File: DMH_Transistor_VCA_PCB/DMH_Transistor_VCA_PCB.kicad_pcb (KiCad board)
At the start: 2 copper layers, 48 x 175 mm, 0 parts

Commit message: Finished main PCB
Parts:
- added C1: 47uF, Capacitor_THT:CP_Radial_D5.0mm_P2.00mm, B.Cu at (73.3, 57.5)
- added C2: 47uF, Capacitor_THT:CP_Radial_D5.0mm_P2.00mm, B.Cu at (90.8, 57.5)
- added C3: 100nF, Capacitor_THT:C_Disc_D4.3mm_W1.9mm_P5.00mm, B.Cu at (69.2, 56.8)
- added C4: 100nF, Capacitor_THT:C_Disc_D4.3mm_W1.9mm_P5.00mm, B.Cu at (97.0, 61.8)
- added C5: 100nF, Capacitor_THT:C_Disc_D4.3mm_W1.9mm_P5.00mm, B.Cu at (89.8, 79.2)
- added C6: 100nF, Capacitor_THT:C_Disc_D4.3mm_W1.9mm_P5.00mm, B.Cu at (76.2, 84.2)
- added C7: 100nF, Capacitor_THT:C_Disc_D4.3mm_W1.9mm_P5.00mm, B.Cu at (89.8, 170.0)
- added C8: 100nF, Capacitor_THT:C_Disc_D4.3mm_W1.9mm_P5.00mm, B.Cu at (76.2, 175.0)
- added D1: SB140+, Diode_THT:D_DO-41_SOD81_P10.16mm_Horizontal, B.Cu at (69.2, 54.3)
- added D2: SB140-, Diode_THT:D_DO-41_SOD81_P10.16mm_Horizontal, B.Cu at (97.0, 44.2)
- added J1: TS_Jack_6.35mm_Sw, SynthStuff:CUI_MJ-63052A, F.Cu at (58.5, 50.8)
- added J100: IDC_02x05, SynthStuff:IDC-Header_2x05_P2.54mm_Vertical_Eurorack, B.Cu at (88.1, 49.0)
- added J2: TS_Jack_6.35mm_Sw, SynthStuff:CUI_MJ-63052A, F.Cu at (58.5, 69.2)
- added J200: IDC_02x05, SynthStuff:IDC-Header_2x05_P2.54mm_Vertical_BackBone, B.Cu at (77.9, 138.2)
- added J3: TS_Jack_6.35mm_Sw, SynthStuff:CUI_MJ-63052A, F.Cu at (63.0, 118.0)
- added J4: TS_Jack_6.35mm_Sw, SynthStuff:CUI_MJ-63052A, F.Cu at (87.0, 118.0)
- added J5: TS_Jack_6.35mm_Sw, SynthStuff:CUI_MJ-63052A, F.Cu at (58.5, 141.5)
- added J50: Conn_01x05, Connector_PinSocket_2.54mm:PinSocket_1x05_P2.54mm_Vertical, F.Cu at (97.0, 76.1)
- added J6: TS_Jack_6.35mm_Sw, SynthStuff:CUI_MJ-63052A, F.Cu at (58.5, 160.0)
- added J60: Conn_01x05, Connector_PinSocket_2.54mm:PinSocket_1x05_P2.54mm_Vertical, F.Cu at (53.0, 187.9)
- added J7: TS_Jack_6.35mm_Sw, SynthStuff:CUI_MJ-63052A, F.Cu at (63.0, 208.8)
- added J8: TS_Jack_6.35mm_Sw, SynthStuff:CUI_MJ-63052A, F.Cu at (87.0, 208.8)
- added Q1: BC548, Package_TO_SOT_THT:TO-92L_Inline_Wide, B.Cu at (81.0, 103.5)
- added Q2: BC548, Package_TO_SOT_THT:TO-92L_Inline_Wide, B.Cu at (85.0, 108.5)
- added Q3: BC548, Package_TO_SOT_THT:TO-92L_Inline_Wide, B.Cu at (85.0, 199.3)
- added Q4: BC548, Package_TO_SOT_THT:TO-92L_Inline_Wide, B.Cu at (81.0, 194.2)
- added R1: 100k, Resistor_THT:R_Axial_DIN0207_L6.3mm_D2.5mm_P7.62mm_Horizontal, B.Cu at (79.2, 63.0)
- added R10: 100R, Resistor_THT:R_Axial_DIN0207_L6.3mm_D2.5mm_P7.62mm_Horizontal, B.Cu at (79.2, 92.7)
- added R11: 100k, Resistor_THT:R_Axial_DIN0207_L6.3mm_D2.5mm_P7.62mm_Horizontal, B.Cu at (75.3, 100.2)
- added R12: 100k, Resistor_THT:R_Axial_DIN0207_L6.3mm_D2.5mm_P7.62mm_Horizontal, B.Cu at (86.8, 92.7)
- added R13: 100R, Resistor_THT:R_Axial_DIN0207_L6.3mm_D2.5mm_P7.62mm_Horizontal, B.Cu at (83.0, 92.7)
- added R14: 20k, Resistor_THT:R_Axial_DIN0207_L6.3mm_D2.5mm_P7.62mm_Horizontal, B.Cu at (94.2, 108.6)
- added R15: 20k, Resistor_THT:R_Axial_DIN0207_L6.3mm_D2.5mm_P7.62mm_Horizontal, B.Cu at (90.8, 108.6)
- added R16: 10k, Resistor_THT:R_Axial_DIN0207_L6.3mm_D2.5mm_P7.62mm_Horizontal, B.Cu at (72.8, 76.7)
- added R17: 10k, Resistor_THT:R_Axial_DIN0207_L6.3mm_D2.5mm_P7.62mm_Horizontal, B.Cu at (69.5, 76.7)
- added R18: 100k, Resistor_THT:R_Axial_DIN0207_L6.3mm_D2.5mm_P7.62mm_Horizontal, B.Cu at (76.0, 65.2)
- added R19: 100k, Resistor_THT:R_Axial_DIN0207_L6.3mm_D2.5mm_P7.62mm_Horizontal, B.Cu at (69.5, 72.8)
- added R2: 100k, Resistor_THT:R_Axial_DIN0207_L6.3mm_D2.5mm_P7.62mm_Horizontal, B.Cu at (86.8, 69.5)
- added R20: 1k, Resistor_THT:R_Axial_DIN0207_L6.3mm_D2.5mm_P7.62mm_Horizontal, B.Cu at (72.8, 72.8)
- added R22: 20k, Resistor_THT:R_Axial_DIN0207_L6.3mm_D2.5mm_P7.62mm_Horizontal, B.Cu at (91.5, 155.7)
- added R23: 20k, Resistor_THT:R_Axial_DIN0207_L6.3mm_D2.5mm_P7.62mm_Horizontal, B.Cu at (94.8, 155.7)
- added R24: 100k, Resistor_THT:R_Axial_DIN0207_L6.3mm_D2.5mm_P7.62mm_Horizontal, B.Cu at (79.2, 160.2)
- added R25: 100k, Resistor_THT:R_Axial_DIN0207_L6.3mm_D2.5mm_P7.62mm_Horizontal, B.Cu at (69.0, 155.9)
- added R26: 10k, Resistor_THT:R_Axial_DIN0207_L6.3mm_D2.5mm_P7.62mm_Horizontal, B.Cu at (69.0, 167.4)
- added R27: 100k, Resistor_THT:R_Axial_DIN0207_L6.3mm_D2.5mm_P7.62mm_Horizontal, B.Cu at (86.8, 157.0)
- added R28: 100k, Resistor_THT:R_Axial_DIN0207_L6.3mm_D2.5mm_P7.62mm_Horizontal, B.Cu at (86.8, 153.8)
- added R29: 1k, Resistor_THT:R_Axial_DIN0207_L6.3mm_D2.5mm_P7.62mm_Horizontal, B.Cu at (75.5, 155.9)
- added R3: 100k, Resistor_THT:R_Axial_DIN0207_L6.3mm_D2.5mm_P7.62mm_Horizontal, B.Cu at (86.8, 66.2)
- added R30: 10k, Resistor_THT:R_Axial_DIN0207_L6.3mm_D2.5mm_P7.62mm_Horizontal, B.Cu at (72.2, 163.6)
- added R31: 100k, Resistor_THT:R_Axial_DIN0207_L6.3mm_D2.5mm_P7.62mm_Horizontal, B.Cu at (72.2, 167.4)
- added R32: 100k, Resistor_THT:R_Axial_DIN0207_L6.3mm_D2.5mm_P7.62mm_Horizontal, B.Cu at (90.0, 186.6)
- added R33: 100k, Resistor_THT:R_Axial_DIN0207_L6.3mm_D2.5mm_P7.62mm_Horizontal, B.Cu at (86.2, 190.8)
- added R34: 100k, Resistor_THT:R_Axial_DIN0207_L6.3mm_D2.5mm_P7.62mm_Horizontal, B.Cu at (83.0, 183.2)
- added R35: 100R, Resistor_THT:R_Axial_DIN0207_L6.3mm_D2.5mm_P7.62mm_Horizontal, B.Cu at (73.8, 190.9)
- added R36: 100R, Resistor_THT:R_Axial_DIN0207_L6.3mm_D2.5mm_P7.62mm_Horizontal, B.Cu at (79.8, 183.2)
- added R37: 100k, Resistor_THT:R_Axial_DIN0207_L6.3mm_D2.5mm_P7.62mm_Horizontal, B.Cu at (93.2, 186.6)
- added R38: 100k, Resistor_THT:R_Axial_DIN0207_L6.3mm_D2.5mm_P7.62mm_Horizontal, B.Cu at (96.5, 178.9)
- added R39: 10k, Resistor_THT:R_Axial_DIN0207_L6.3mm_D2.5mm_P7.62mm_Horizontal, B.Cu at (75.5, 178.9)
- added R4: 100k, Resistor_THT:R_Axial_DIN0207_L6.3mm_D2.5mm_P7.62mm_Horizontal, B.Cu at (90.0, 88.2)
- added R41: 82k, Resistor_THT:R_Axial_DIN0207_L6.3mm_D2.5mm_P7.62mm_Horizontal, B.Cu at (72.2, 186.6)
- added R42: 100k, Resistor_THT:R_Axial_DIN0207_L6.3mm_D2.5mm_P7.62mm_Horizontal, B.Cu at (69.0, 178.9)
- added R5: 100k, Resistor_THT:R_Axial_DIN0207_L6.3mm_D2.5mm_P7.62mm_Horizontal, B.Cu at (93.2, 95.8)
- added R6: 100k, Resistor_THT:R_Axial_DIN0207_L6.3mm_D2.5mm_P7.62mm_Horizontal, B.Cu at (96.5, 95.8)
- added R7: 100k, Resistor_THT:R_Axial_DIN0207_L6.3mm_D2.5mm_P7.62mm_Horizontal, B.Cu at (69.5, 95.8)
- added R8: 82k, Resistor_THT:R_Axial_DIN0207_L6.3mm_D2.5mm_P7.62mm_Horizontal, B.Cu at (76.0, 88.2)
- added R9: 10k, Resistor_THT:R_Axial_DIN0207_L6.3mm_D2.5mm_P7.62mm_Horizontal, B.Cu at (72.8, 88.2)
- added RV4: 100k, Potentiometer_THT:Potentiometer_Bourns_3296W_Vertical, B.Cu at (92.2, 64.5)
- added RV6: 100k, Potentiometer_THT:Potentiometer_Bourns_3296W_Vertical, B.Cu at (95.5, 168.5)
- added U1: TL074, Package_DIP:DIP-14_W7.62mm_Socket, B.Cu at (86.8, 72.9)
- added U2: TL074, Package_DIP:DIP-14_W7.62mm_Socket, B.Cu at (86.8, 163.6)
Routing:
- net -12V: track 0.00 -> 183.8 mm
- net +12V: track 0.00 -> 164.6 mm
- net Net-(J200-Pin_2): track 0.00 -> 126.8 mm
- net /Core Circuit B/CV 1 B Input: track 0.00 -> 101.6 mm
- net Net-(J200-Pin_1): track 0.00 -> 101.0 mm
- net Net-(J200-Pin_7): track 0.00 -> 88.2 mm
- net /Core Circuit B/CV 2 B Pot: track 0.00 -> 81.8 mm
- net Net-(Q4-C): track 0.00 -> 80.9 mm
- net Net-(Q1-C): track 0.00 -> 79.5 mm
- net Net-(J200-Pin_6): track 0.00 -> 78.1 mm
- net Net-(Q3-C): track 0.00 -> 76.3 mm
- net Net-(Q2-C): track 0.00 -> 65.3 mm
- net Net-(U2C--): track 0.00 -> 65.1 mm
- net Net-(U1C--): track 0.00 -> 62.6 mm
- net /Core Circuit B/Input B: track 0.00 -> 61.5 mm
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- added copper zone on B.Cu, net GND
- added copper zone on F.Cu, net GND

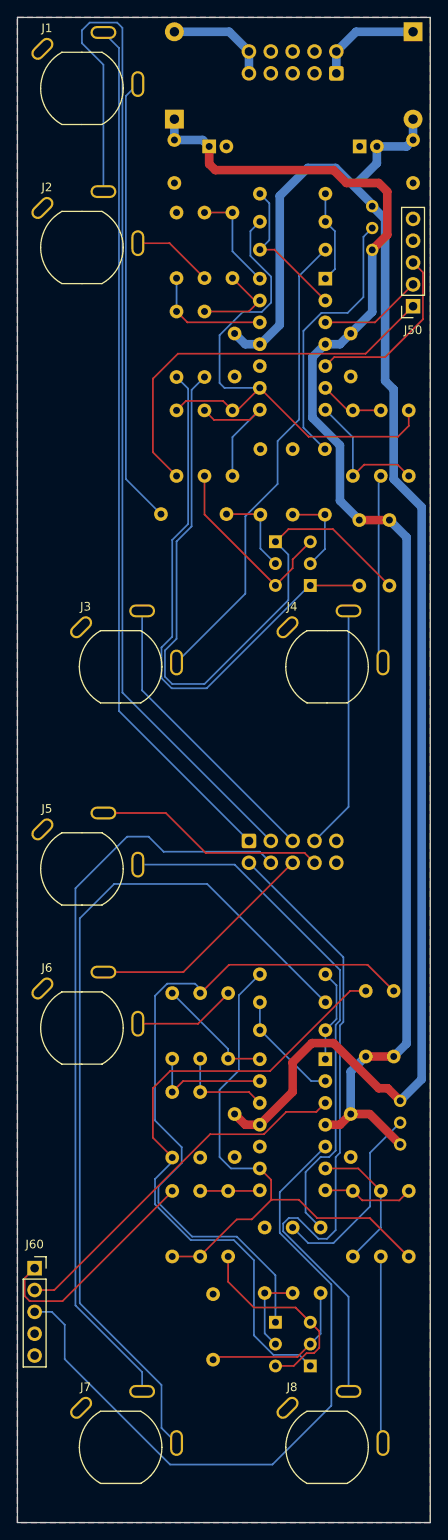
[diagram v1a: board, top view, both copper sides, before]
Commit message: Pots PCB in progress
Need to add CV input traces to the pin headers
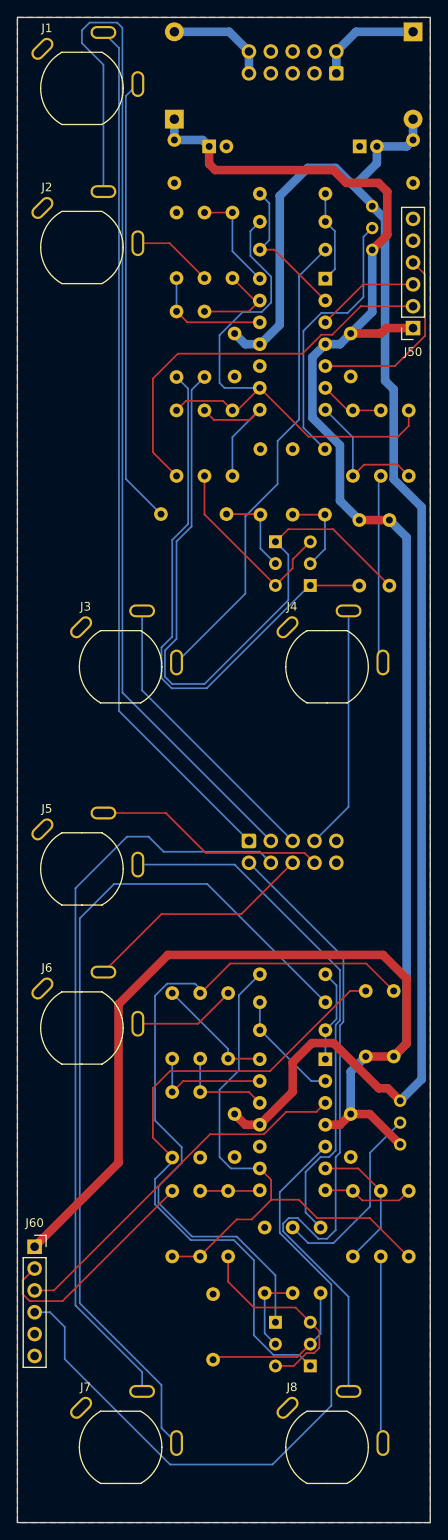
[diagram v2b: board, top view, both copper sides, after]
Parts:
- J50, J60: value Conn_01x05 -> Conn_01x06; footprint Connector_PinSocket_2.54mm:PinSocket_1x05_P2.54mm_Vertical -> Connector_PinSocket_2.54mm:PinSocket_1x06_P2.54mm_Vertical
- moved J50 2.54 mm to (97.0, 78.6)
- moved J60 2.49 mm to (53.0, 185.4)
- renumbered RV4 to RV7, RV6 to RV8
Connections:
- J50 pad 1: /Core Circuit A/Offset A Pot -> +12V
- J50 pad 2: /Core Circuit A/CV 1 A Pot -> /Core Circuit A/Offset A Pot
- J50 pad 3: /Core Circuit A/CV 2 A Pot -> /Core Circuit A/CV 1 A Pot
- J50 pad 4: GND -> /Core Circuit A/CV 2 A Pot
- J60 pad 1: /Core Circuit B/Offset B Pot -> +12V
- J60 pad 2: /Core Circuit B/CV 1 B Pot -> /Core Circuit B/Offset B Pot
- J60 pad 3: /Core Circuit B/CV 2 B Pot -> /Core Circuit B/CV 1 B Pot
- J60 pad 4: GND -> /Core Circuit B/CV 2 B Pot
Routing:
- net +12V: track 164.6 -> 251.0 mm
- net /Core Circuit A/CV 2 A Pot: track 20.7 -> 22.2 mm

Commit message: Finished Pots PCB
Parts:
- J50, J60: value Conn_01x06 -> Conn_01x08; footprint Connector_PinSocket_2.54mm:PinSocket_1x06_P2.54mm_Vertical -> Connector_PinSocket_2.54mm:PinSocket_1x08_P2.54mm_Vertical
- moved J60 5.05 mm to (53.0, 180.4)
- moved J50 5.00 mm to (97.0, 83.6)
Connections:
- J50 pad 1: +12V -> /Core Circuit A/CV 1 A Input
- J50 pad 2: /Core Circuit A/Offset A Pot -> /Core Circuit A/CV 2 A Input
- J50 pad 3: /Core Circuit A/CV 1 A Pot -> +12V
- J50 pad 4: /Core Circuit A/CV 2 A Pot -> /Core Circuit A/Offset A Pot
- J50 pad 5: GND -> /Core Circuit A/CV 1 A Pot
- J50 pad 6: GND -> /Core Circuit A/CV 2 A Pot
- J60 pad 1: +12V -> /Core Circuit B/CV 1 B Input
- J60 pad 2: /Core Circuit B/Offset B Pot -> /Core Circuit B/CV 2 B Input
- J60 pad 3: /Core Circuit B/CV 1 B Pot -> +12V
- J60 pad 4: /Core Circuit B/CV 2 B Pot -> /Core Circuit B/Offset B Pot
- J60 pad 5: GND -> /Core Circuit B/CV 1 B Pot
- J60 pad 6: GND -> /Core Circuit B/CV 2 B Pot
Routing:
- net /Core Circuit B/CV 2 B Input: track 21.8 -> 98.6 mm
- net /Core Circuit A/CV 1 A Input: track 55.2 -> 112.9 mm
- net /Core Circuit B/CV 1 B Input: track 101.6 -> 136.7 mm
- net /Core Circuit A/CV 2 A Input: track 22.0 -> 43.4 mm

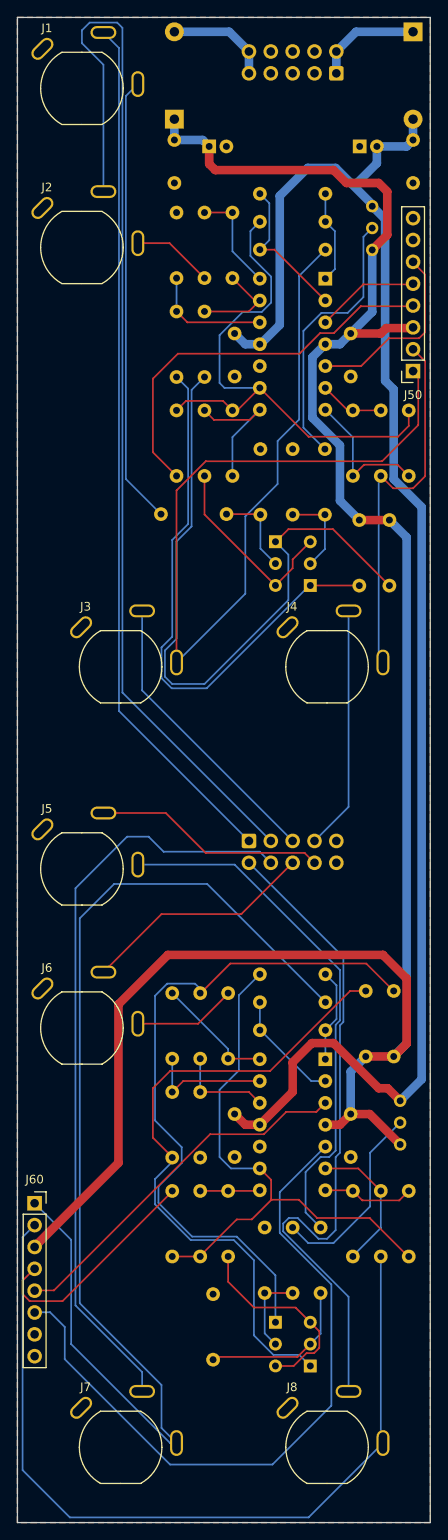
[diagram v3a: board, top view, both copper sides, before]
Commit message: Added CV input attenuverter adjustment trimpots
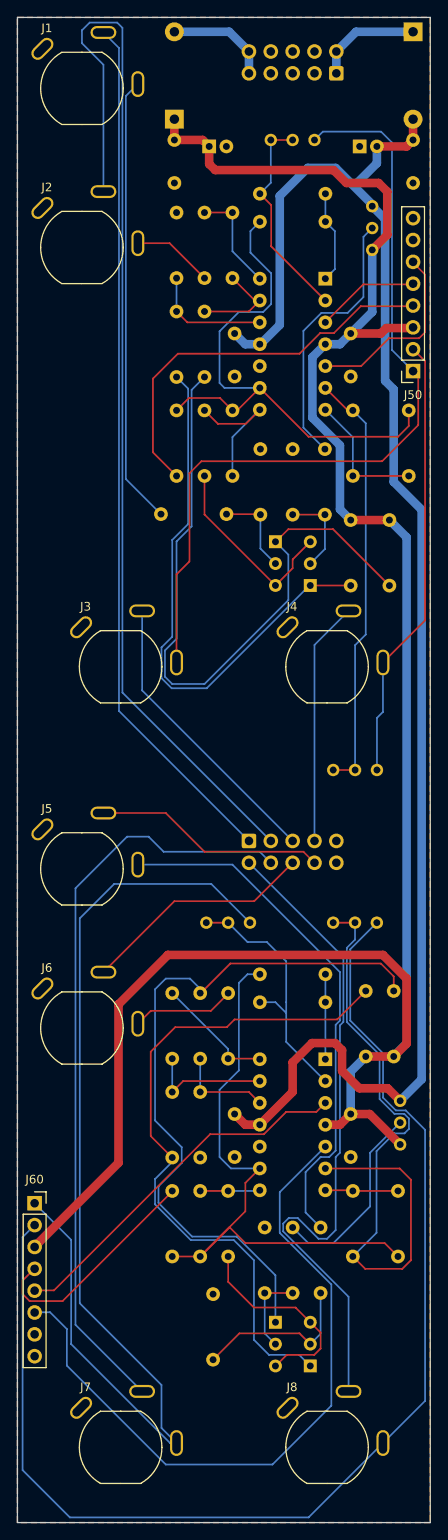
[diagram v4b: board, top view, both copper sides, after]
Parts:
- removed R2, R27, R37, R5: 100k, Resistor_THT:R_Axial_DIN0207_L6.3mm_D2.5mm_P7.62mm_Horizontal
- added RV10: 50k, Potentiometer_THT:Potentiometer_Bourns_3296W_Vertical, B.Cu at (92.8, 130.0)
- added RV11: 50k, Potentiometer_THT:Potentiometer_Bourns_3296W_Vertical, B.Cu at (78.0, 147.8)
- added RV12: 50k, Potentiometer_THT:Potentiometer_Bourns_3296W_Vertical, B.Cu at (92.8, 147.8)
- added RV9: 50k, Potentiometer_THT:Potentiometer_Bourns_3296W_Vertical, B.Cu at (85.5, 56.8)
- R1, R24, R32, R4: value 100k -> 33k
- moved R24 3.25 mm to (79.2, 157.0)
- moved R38 1.25 mm to (95.2, 178.9)
- moved R15 1.00 mm to (89.8, 108.6)
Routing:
- net Net-(U2B--): track 16.5 -> 76.4 mm
- net /Core Circuit B/CV 2 B Input: track 98.6 -> 144.9 mm
- net Net-(U1B--): track 7.53 -> 49.8 mm
- net Net-(U2A--): track 13.3 -> 30.5 mm
- net /Core Circuit A/CV 1 A Input: track 112.9 -> 95.8 mm
- net /Core Circuit B/CV 1 B Input: track 136.7 -> 124.1 mm
- net /Core Circuit A/CV 2 A Input: track 43.4 -> 51.5 mm
- net Net-(U1A--): track 17.5 -> 25.1 mm
- net Net-(U2C--): track 65.1 -> 71.4 mm
- net Net-(Q3-C): track 76.3 -> 79.0 mm
- net Net-(R32-Pad2): track 10.6 -> 8.48 mm
- net Net-(Q4-C): track 81.0 -> 82.9 mm
- net -12V: track 183.8 -> 185.2 mm
- net Net-(R4-Pad2): track 16.6 -> 15.5 mm
- net Net-(R24-Pad2): track 10.9 -> 9.88 mm
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
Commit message: Switched attenuverters trimpot and Rf positions
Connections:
- R1 pad 1: Net-(U1A--) -> /Core Circuit A/CV 1 A Input
- R1 pad 2: Net-(R1-Pad2) -> Net-(U1A--)
- R24 pad 1: Net-(U2A--) -> /Core Circuit B/CV 1 B Input
- R24 pad 2: Net-(R24-Pad2) -> Net-(U2A--)
- R28 pad 1: Net-(R24-Pad2) -> Net-(R28-Pad1)
- R3 pad 1: Net-(R1-Pad2) -> Net-(R3-Pad1)
- R32 pad 1: Net-(U2B--) -> /Core Circuit B/CV 2 B Input
- R32 pad 2: Net-(R32-Pad2) -> Net-(U2B--)
- R38 pad 1: Net-(R32-Pad2) -> Net-(R38-Pad1)
- R4 pad 1: Net-(U1B--) -> /Core Circuit A/CV 2 A Input
- R4 pad 2: Net-(R4-Pad2) -> Net-(U1B--)
- R6 pad 1: Net-(R4-Pad2) -> Net-(R6-Pad1)
- RV10 pad 1: /Core Circuit A/CV 2 A Input -> Net-(U1B--)
- RV10 pad 2: Net-(U1B--) -> Net-(R6-Pad1)
- RV10 pad 3: Net-(U1B--) -> Net-(R6-Pad1)
- RV11 pad 1: /Core Circuit B/CV 1 B Input -> Net-(U2A--)
- RV11 pad 2: Net-(U2A--) -> Net-(R28-Pad1)
- RV11 pad 3: Net-(U2A--) -> Net-(R28-Pad1)
- RV12 pad 1: /Core Circuit B/CV 2 B Input -> Net-(U2B--)
- RV12 pad 2: Net-(U2B--) -> Net-(R38-Pad1)
- RV12 pad 3: Net-(U2B--) -> Net-(R38-Pad1)
- RV9 pad 1: /Core Circuit A/CV 1 A Input -> Net-(U1A--)
- RV9 pad 2: Net-(U1A--) -> Net-(R3-Pad1)
- RV9 pad 3: Net-(U1A--) -> Net-(R3-Pad1)
- U1 pad 1: Net-(R1-Pad2) -> Net-(R3-Pad1)
- U1 pad 7: Net-(R4-Pad2) -> Net-(R6-Pad1)
- U2 pad 1: Net-(R24-Pad2) -> Net-(R28-Pad1)
- U2 pad 7: Net-(R32-Pad2) -> Net-(R38-Pad1)
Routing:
- net Net-(R6-Pad1): track 0.00 -> 66.4 mm
- net Net-(R38-Pad1): track 0.00 -> 49.9 mm
- net /Core Circuit B/CV 2 B Input: track 144.9 -> 100.0 mm
- net Net-(U2B--): track 76.4 -> 36.6 mm
- net /Core Circuit B/CV 1 B Input: track 124.1 -> 88.3 mm
- net Net-(R3-Pad1): track 0.00 -> 29.1 mm
- net Net-(R28-Pad1): track 0.00 -> 28.5 mm
- net Net-(R4-Pad2): track 15.5 -> 0.00 mm
- net Net-(U1A--): track 25.1 -> 36.9 mm
- net Net-(R1-Pad2): track 10.8 -> 0.00 mm
- net Net-(R24-Pad2): track 9.88 -> 0.00 mm
- net /Core Circuit A/CV 1 A Input: track 95.8 -> 105.7 mm
- net -12V: track 185.2 -> 176.0 mm
- net Net-(R32-Pad2): track 8.48 -> 0.00 mm
- net Net-(U2A--): track 30.5 -> 23.1 mm
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
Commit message: Changed R8 and R41 to 100k
... in order to remove gain reduction of the incoming CV and offset
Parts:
- R41, R8: value 82k -> 100k

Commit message: Generated Gerbers
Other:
- board text added: "Mk1.0 - March 2025"
- board text removed: "Mk1.0 - Month Year"
